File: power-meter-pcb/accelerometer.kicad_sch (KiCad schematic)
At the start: 2 parts

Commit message: Assigning footprints, extremely rough idea of size
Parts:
- C4: footprint (none) -> Capacitor_SMD:C_0603_1608Metric_Pad1.08x0.95mm_HandSolder
- MT1: footprint ICM-42670-P:XDCR_ICM-42670-P -> ICM-42670-P_AccelGyro:XDCR_ICM-42670-P
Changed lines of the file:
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@@
 			)
 		)
-		(property "Footprint" "ICM-42670-P:XDCR_ICM-42670-P"
+		(property "Footprint" "ICM-42670-P_AccelGyro:XDCR_ICM-42670-P"
 			(at 158.75 96.52 0)
 			(effects
@@
 			)
 		)
-		(property "Footprint" ""
+		(property "Footprint" "Capacitor_SMD:C_0603_1608Metric_Pad1.08x0.95mm_HandSolder"
 			(at 213.0552 102.87 0)
 			(effects

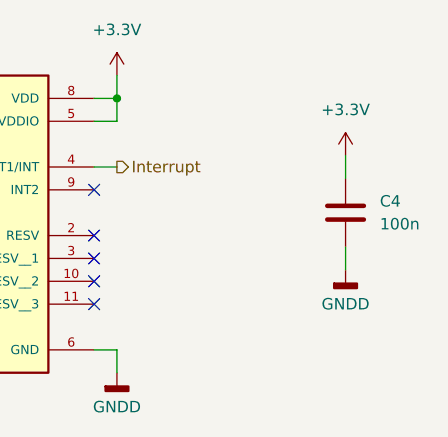
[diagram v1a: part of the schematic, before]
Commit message: Added power supply to PCB
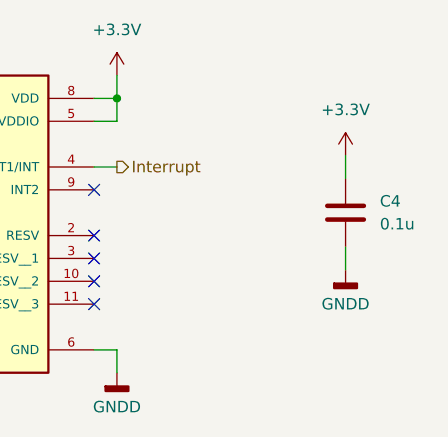
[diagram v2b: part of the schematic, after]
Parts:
- C4: value 100n -> 0.1u
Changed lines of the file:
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@@
 			)
 		)
-		(property "Value" "100n"
+		(property "Value" "0.1u"
 			(at 215.9 100.3299 0)
 			(effects

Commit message: Started PCB layout
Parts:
- renumbered C4 to C14
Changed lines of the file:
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@@
 		(dnp no)
 		(fields_autoplaced yes)
-		(property "Reference" "#PWR027"
+		(property "Reference" "#PWR044"
 			(at 212.09 111.76 0)
 			(effects
@@
 			(project "power-meter-pcb"
 				(path "/73d1dc3f-3725-4767-8c11-2d32e15ee0d6/2b9cb85e-d958-4741-88c2-27e776d7a0b9"
-					(reference "#PWR027")
+					(reference "#PWR044")
 					(unit 1)
 				)
@@
 		(dnp no)
 		(fields_autoplaced yes)
-		(property "Reference" "#PWR028"
+		(property "Reference" "#PWR043"
 			(at 212.09 96.52 0)
 			(effects
@@
 			(project "power-meter-pcb"
 				(path "/73d1dc3f-3725-4767-8c11-2d32e15ee0d6/2b9cb85e-d958-4741-88c2-27e776d7a0b9"
-					(reference "#PWR028")
+					(reference "#PWR043")
 					(unit 1)
 				)
@@
 		(dnp no)
 		(fields_autoplaced yes)
-		(property "Reference" "#PWR025"
+		(property "Reference" "#PWR042"
 			(at 186.69 123.19 0)
 			(effects
@@
 			(project "power-meter-pcb"
 				(path "/73d1dc3f-3725-4767-8c11-2d32e15ee0d6/2b9cb85e-d958-4741-88c2-27e776d7a0b9"
-					(reference "#PWR025")
+					(reference "#PWR042")
 					(unit 1)
 				)
@@
 		(dnp no)
 		(fields_autoplaced yes)
-		(property "Reference" "#PWR026"
+		(property "Reference" "#PWR041"
 			(at 186.69 87.63 0)
 			(effects
@@
 			(project "power-meter-pcb"
 				(path "/73d1dc3f-3725-4767-8c11-2d32e15ee0d6/2b9cb85e-d958-4741-88c2-27e776d7a0b9"
-					(reference "#PWR026")
+					(reference "#PWR041")
 					(unit 1)
 				)
@@
 		(dnp no)
 		(fields_autoplaced yes)
-		(property "Reference" "C4"
+		(property "Reference" "C14"
 			(at 215.9 97.7899 0)
 			(effects
@@
 			(project "power-meter-pcb"
 				(path "/73d1dc3f-3725-4767-8c11-2d32e15ee0d6/2b9cb85e-d958-4741-88c2-27e776d7a0b9"
-					(reference "C4")
+					(reference "C14")
 					(unit 1)
 				)
@@
 		(dnp no)
 		(fields_autoplaced yes)
-		(property "Reference" "#PWR029"
+		(property "Reference" "#PWR040"
 			(at 115.57 100.33 0)
 			(effects
@@
 			(project "power-meter-pcb"
 				(path "/73d1dc3f-3725-4767-8c11-2d32e15ee0d6/2b9cb85e-d958-4741-88c2-27e776d7a0b9"
-					(reference "#PWR029")
-					(unit 1)
-				)
+					(reference "#PWR040")
+					(unit 1)
+				)

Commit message: Routing and component placement continues
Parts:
- renumbered C14 to C16
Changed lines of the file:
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@@
+	(bus
+		(pts
+			(xy 120.65 97.79) (xy 120.65 99.06)
+		)
+		(stroke
+			(width 0)
+			(type default)
+		)
+	)
 	(bus
 		(pts
@@
 		(dnp no)
 		(fields_autoplaced yes)
-		(property "Reference" "#PWR044"
+		(property "Reference" "#PWR046"
 			(at 212.09 111.76 0)
 			(effects
@@
 			(project "power-meter-pcb"
 				(path "/73d1dc3f-3725-4767-8c11-2d32e15ee0d6/2b9cb85e-d958-4741-88c2-27e776d7a0b9"
-					(reference "#PWR044")
+					(reference "#PWR046")
 					(unit 1)
 				)
@@
 		(dnp no)
 		(fields_autoplaced yes)
-		(property "Reference" "#PWR043"
+		(property "Reference" "#PWR045"
 			(at 212.09 96.52 0)
 			(effects
@@
 			(project "power-meter-pcb"
 				(path "/73d1dc3f-3725-4767-8c11-2d32e15ee0d6/2b9cb85e-d958-4741-88c2-27e776d7a0b9"
-					(reference "#PWR043")
+					(reference "#PWR045")
 					(unit 1)
 				)
@@
 		(dnp no)
 		(fields_autoplaced yes)
-		(property "Reference" "#PWR042"
+		(property "Reference" "#PWR044"
 			(at 186.69 123.19 0)
 			(effects
@@
 			(project "power-meter-pcb"
 				(path "/73d1dc3f-3725-4767-8c11-2d32e15ee0d6/2b9cb85e-d958-4741-88c2-27e776d7a0b9"
-					(reference "#PWR042")
+					(reference "#PWR044")
 					(unit 1)
 				)
@@
 		(dnp no)
 		(fields_autoplaced yes)
-		(property "Reference" "#PWR041"
+		(property "Reference" "#PWR043"
 			(at 186.69 87.63 0)
 			(effects
@@
 			(project "power-meter-pcb"
 				(path "/73d1dc3f-3725-4767-8c11-2d32e15ee0d6/2b9cb85e-d958-4741-88c2-27e776d7a0b9"
-					(reference "#PWR041")
+					(reference "#PWR043")
 					(unit 1)
 				)
@@
 		(dnp no)
 		(fields_autoplaced yes)
-		(property "Reference" "C14"
+		(property "Reference" "C16"
 			(at 215.9 97.7899 0)
 			(effects
@@
 			(project "power-meter-pcb"
 				(path "/73d1dc3f-3725-4767-8c11-2d32e15ee0d6/2b9cb85e-d958-4741-88c2-27e776d7a0b9"
-					(reference "C14")
+					(reference "C16")
 					(unit 1)
 				)
@@
 		(dnp no)
 		(fields_autoplaced yes)
-		(property "Reference" "#PWR040"
+		(property "Reference" "#PWR042"
 			(at 115.57 100.33 0)
 			(effects
@@
 			(project "power-meter-pcb"
 				(path "/73d1dc3f-3725-4767-8c11-2d32e15ee0d6/2b9cb85e-d958-4741-88c2-27e776d7a0b9"
-					(reference "#PWR040")
+					(reference "#PWR042")
 					(unit 1)
 				)

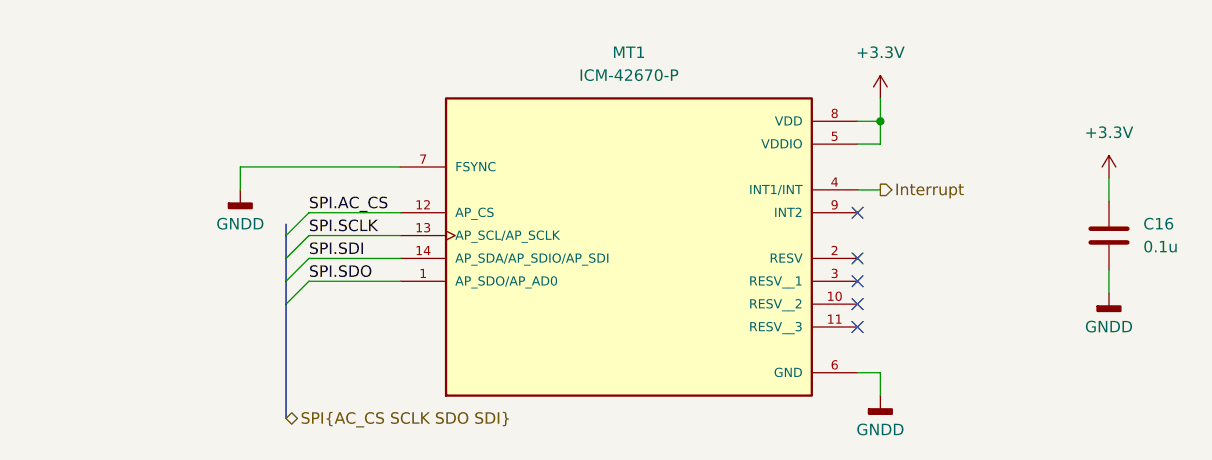
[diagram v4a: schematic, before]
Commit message: Tidying schematic
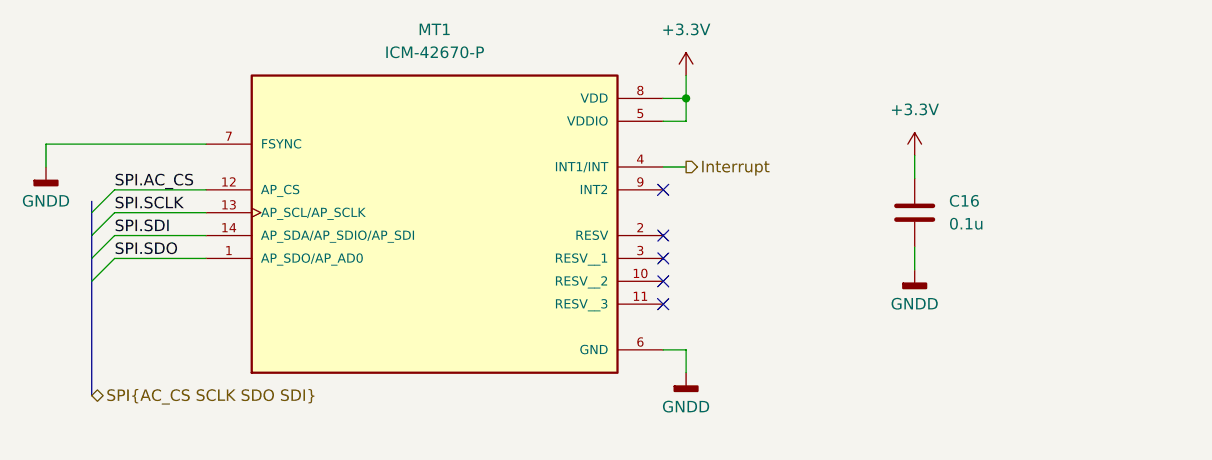
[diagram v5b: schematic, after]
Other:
- moved on the sheet: C16, MT1

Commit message: Cleaning up PCB back and title box
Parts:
- C16, MT1: PlaceOnSecondary (none) -> No
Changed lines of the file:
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@@
 	(title_block
 		(title "Cycling power meter FYP - Accelerometer and gyroscope")
-		(date "2024-04-18")
+		(date "2024-05-14")
+		(rev "V1.0")
 		(company "Monash Human Power - Jotham Gates & Oscar Varney")
-		(comment 1 "For the secondary crank, set J3 to short pins 2 and 3 and short J1 and J2.")
 	)
 	(junction
@@
 			)
 		)
-		(property "Description" ""
+		(property "Description" "Accelerometer and gyroscope"
 			(at 137.16 93.98 0)
 			(effects
@@
 				)
 				(justify bottom)
+				(hide yes)
+			)
+		)
+		(property "PlaceOnSecondary" "No"
+			(at 137.16 93.98 0)
+			(effects
+				(font
+					(size 1.27 1.27)
+				)
 				(hide yes)
 			)
@@
 			(at 190.5 96.52 0)
 			(effects
+				(font
+					(size 1.27 1.27)
+				)
+				(hide yes)
+			)
+		)
+		(property "PlaceOnSecondary" "No"
+			(at 190.5 96.52 0)
+			(effects
